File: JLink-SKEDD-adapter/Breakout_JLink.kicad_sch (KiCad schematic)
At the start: 7 parts, among them J1 UART_ClientSide, J2 Conn_02x10_Odd_Even, J3 Jitter_Debug_HostSide, J4 Conn_01x06_Female

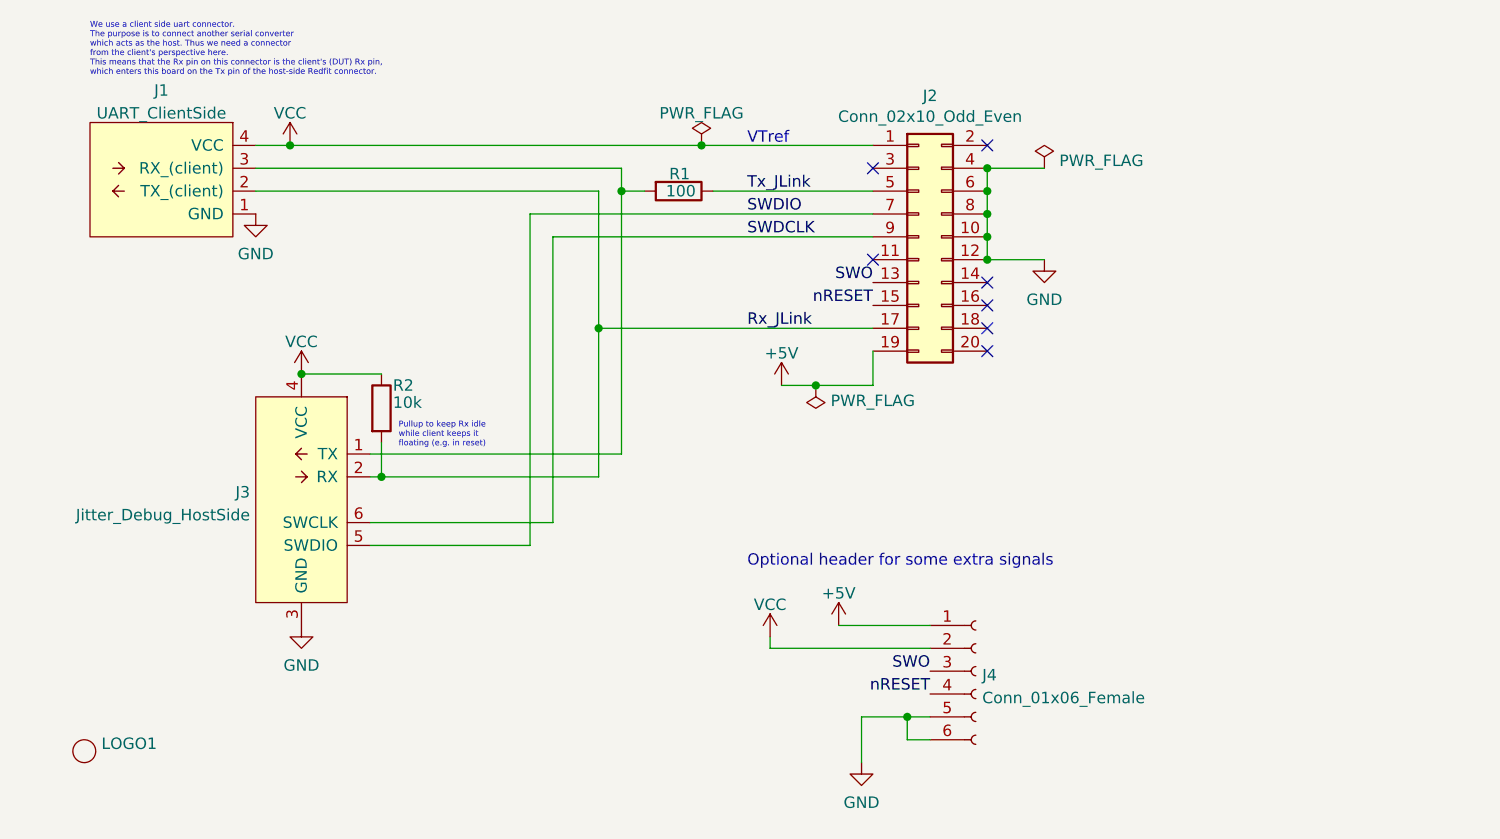
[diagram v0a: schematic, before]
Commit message: Update JLink SKEDD breakout to Kicad 10
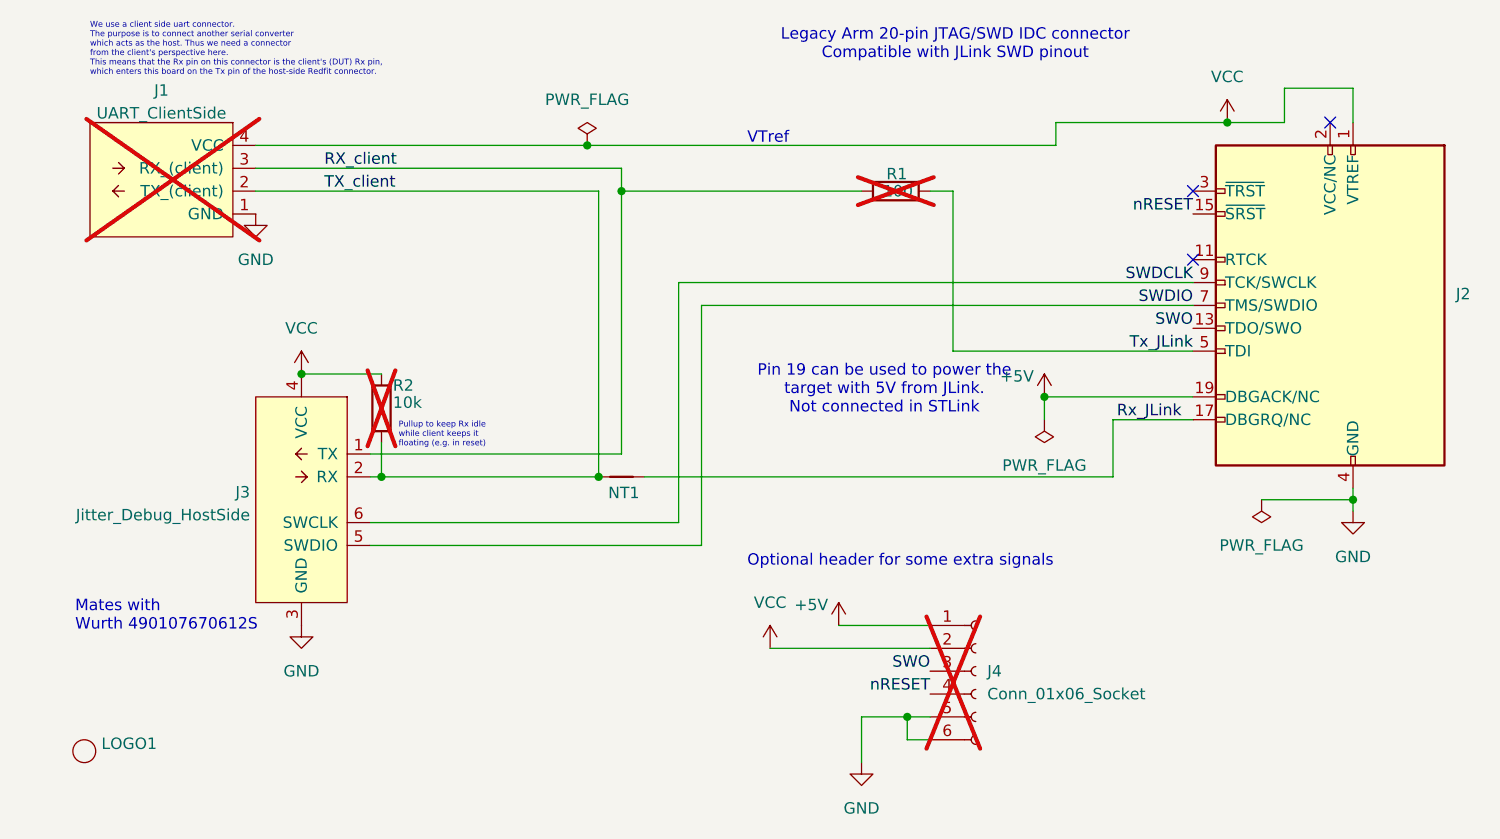
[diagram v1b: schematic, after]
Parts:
- removed J2: Conn_02x10_Odd_Even, Jitter_Connectors:JLink_PinHeader_2x10_2.54_Horizontal, symbol Connector_Generic:Conn_02x10_Odd_Even
- removed J4: Conn_01x06_Female, Connector_PinHeader_2.54mm:PinHeader_1x06_P2.54mm_Vertical, symbol Connector:Conn_01x06_Female
- added J2: 2x10 female header 2.54mm pitch. With a notch/key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, Jitter_Connectors:JLink_PinHeader_2x10_2.54_Horizontal, symbol Connector:Conn_ARM_JTAG_SWD_20
- added J4: Conn_01x06_Socket, Connector_PinHeader_2.54mm:PinHeader_1x06_P2.54mm_Vertical, symbol Connector:Conn_01x06_Socket
- added NT1: NetTie_2, Jitter_Footprints:NetTie-2_SMD_Pad0.2mm, symbol Device:NetTie_2
- J1, R1, R2: now not fitted
- J3, LOGO1: now left out of the parts list
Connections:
- net +5V: now also J2.19 (DBGACK/NC), J4.1 (Pin_1)
- net GND: now also J2.10 (GND), J2.12 (GND), J2.14 (GND), J2.16 (GND), J2.18 (GND), J2.20 (GND), J2.4 (GND), J2.6 (GND), J2.8 (GND), J4.5 (Pin_5), J4.6 (Pin_6)
- net Rx_JLink: now also J2.17 (DBGRQ/NC), NT1.2; no longer J1.2 (TX_(client)), J3.2 (RX), R2.2
- net SWDCLK: now also J2.9 (TCK/SWCLK)
- net SWDIO: now also J2.7 (TMS/SWDIO)
- net SWO: now also J2.13 (TDO/SWO), J4.3 (Pin_3)
- net Tx_JLink: now also J2.5 (TDI)
- net VCC: now also J2.1 (VTREF), J4.2 (Pin_2)
- net nRESET: now also J2.15 (~{SRST}), J4.4 (Pin_4)
- net RX_client: now reaches J1.3 (RX_(client)), J3.1 (TX), R1.2
- new net TX_client: J1.2 (TX_(client)), J3.2 (RX), NT1.1, R2.2
- no-connect marks 7 -> 3
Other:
- note added: "Legacy Arm 20-pin JTAG/SWD IDC connector Compatible with JLink SWD pinout"
- note added: "Mates with Wurth 490107670612S"
- note added: "Pin 19 can be used to power the target with 5V from JLink. Not connected in STLink"
